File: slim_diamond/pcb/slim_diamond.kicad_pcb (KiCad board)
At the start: 2 copper layers, 87.4 x 92.1 mm, 25 parts, among them J1 JST PH 2.0 battery, SW1 pinky, SW10 index_bottom, SW11 thumb_outer, SW12 thumb_inner, SW13 MSK-12C02, SW2 ring_top, SW3 ring_home, SW4 ring_bottom, SW5 middle_top, SW6 middle_home, SW7 middle_bottom, SW8 index_top, SW9 index_home, U1 XIAO nRF52840

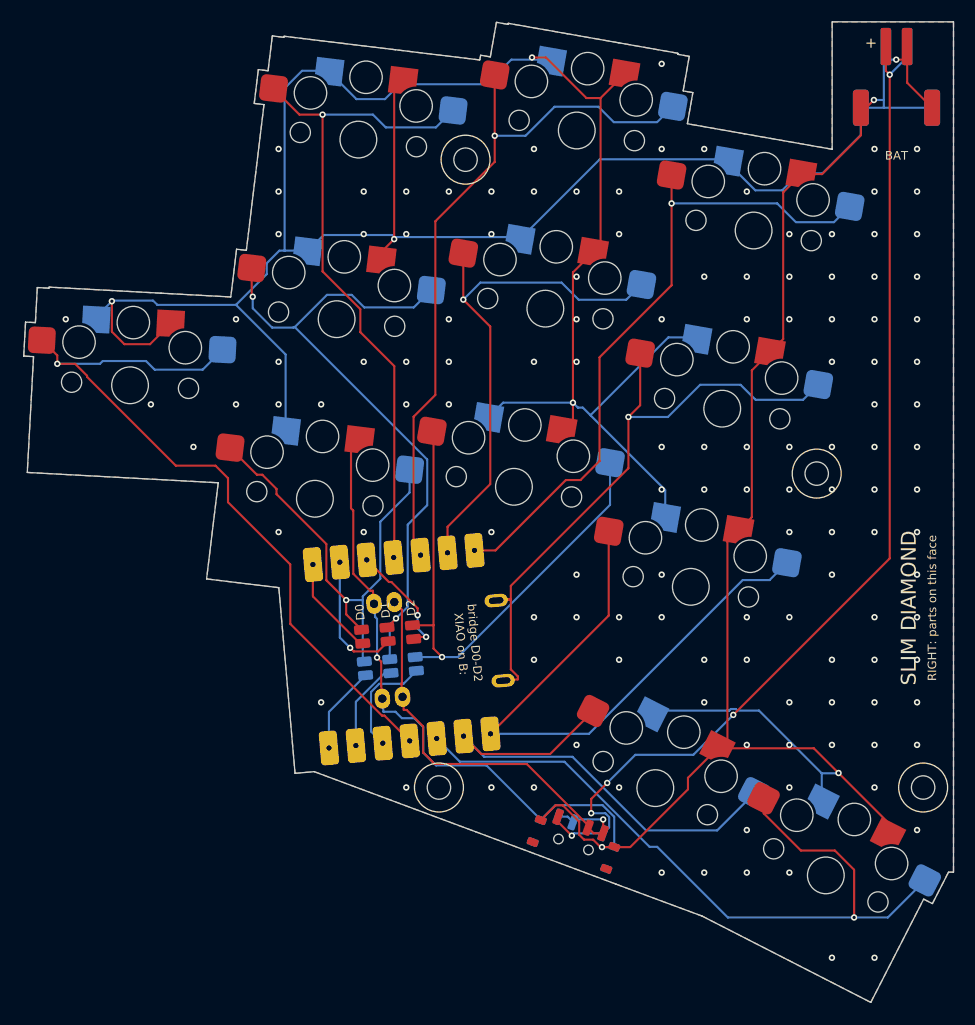
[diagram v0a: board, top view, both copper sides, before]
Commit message: Shape the Slim Diamond like a diamond, joined or stacked
Side by side, the joined halves are now a cut-diamond silhouette: the
fewest-facet convex outline around both halves, a table at the back and
pavilion facets down to the thumbs. The PCB follows it too. Stacked back
to back, the case walls lean in from a floor 2 mm wider than the rim, so
the pair reads as a cut gem from the side. Each half grows about 10%, the
PCB still fits JLC's 100 mm tier, and the tent stays at 6.6 degrees.

The Xiao and power switch move to the lower outer facet, with a routing
channel around both. A spot the router can't finish falls back to the
search's runners-up. The tent search now treats parts past the outermost
key as infeasible, and places the JST by least tent. New renders show
the halves joined and stacked.

Co-Authored-By: Claude Opus 5.5 <noreply@anthropic.com>
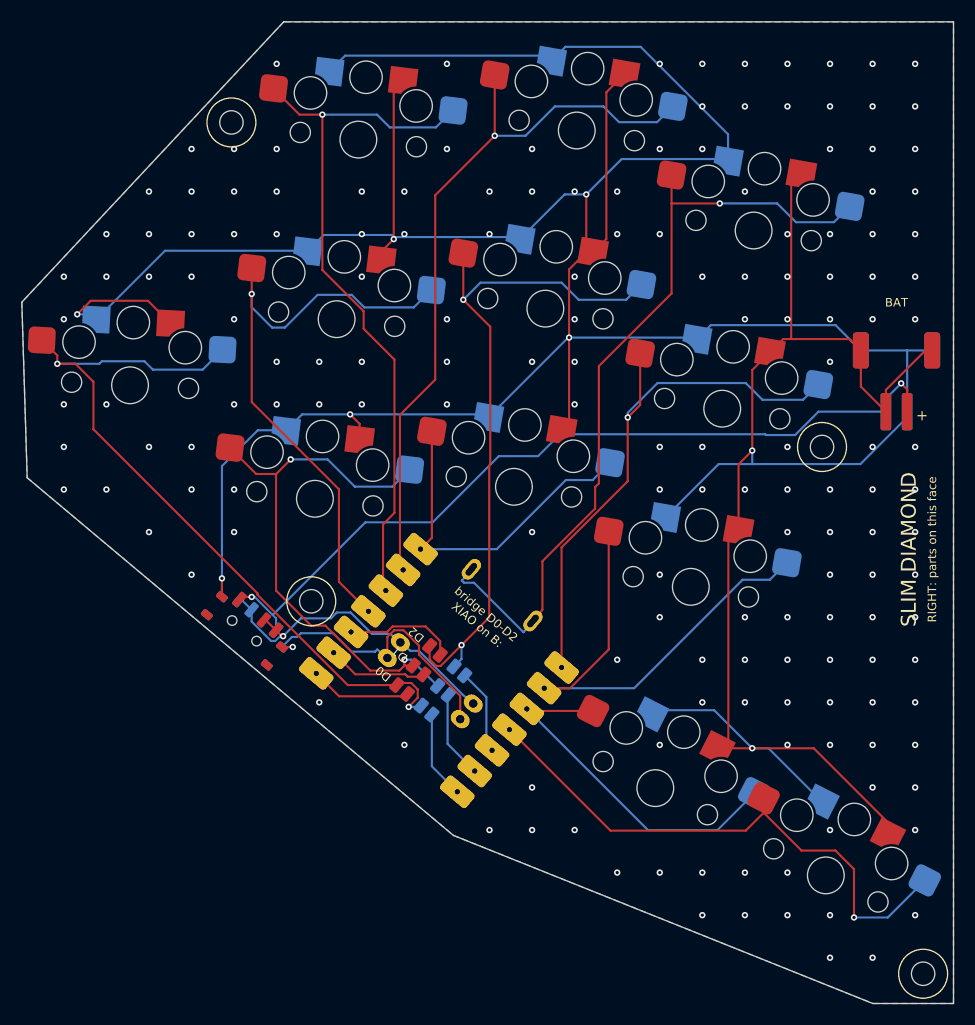
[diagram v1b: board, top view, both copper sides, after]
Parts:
- moved H4 49.0 mm to (78.0, 127.5)
- moved H3 48.2 mm to (126.0, 113.0)
- moved SW13 36.9 mm to (71.7, 130.3), turned to -40 degrees
- moved J1 28.6 mm to (133.0, 106.8), turned to 180 degrees
- moved H2 22.3 mm to (70.5, 82.5)
- moved H1 17.5 mm to (135.5, 162.5)
- moved JP14 6.99 mm to (88.8, 137.7), turned to 140 degrees
- moved JP1 6.23 mm to (86.5, 135.8), turned to 140 degrees
- moved JP13 5.44 mm to (90.4, 135.9), turned to 140 degrees
- moved JP2 4.43 mm to (88.1, 134.0), turned to 140 degrees
- moved JP12 4.15 mm to (91.9, 134.0), turned to 140 degrees
- moved U1 4.03 mm to (90.0, 134.0), turned to 140 degrees
- moved JP3 2.68 mm to (89.6, 132.1), turned to 140 degrees
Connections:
- JP1 pad 2: K_ring_bottom -> K_pinky
- JP12 pad 2: K_middle_bottom -> K_middle_home
- JP13 pad 2: K_ring_home -> K_ring_bottom
- JP14 pad 2: K_ring_bottom -> K_pinky
- JP2 pad 2: K_ring_home -> K_ring_bottom
- JP3 pad 2: K_middle_bottom -> K_middle_home
- U1 pad L10: K_thumb_inner -> K_thumb_outer
- U1 pad L11: K_pinky -> K_thumb_inner
- U1 pad L4: K_ring_top -> K_ring_home
- U1 pad L5: K_middle_top -> K_ring_top
- U1 pad L6: K_middle_home -> K_middle_top
- U1 pad L7: K_index_top -> K_middle_bottom
- U1 pad L8: K_index_bottom -> K_index_home
- U1 pad L9: K_thumb_outer -> K_index_bottom
- U1 pad NFC1: K_index_home -> K_index_top
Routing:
- net BAT+: track 99.3 -> 77.3 mm, vias 5 -> 2
- net K_middle_bottom: track 51.8 -> 32.7 mm, vias 1 -> 0
- net K_thumb_inner: track 70.9 -> 53.2 mm
- net K_middle_home: track 49.5 -> 65.3 mm, vias 1 -> 2
- net GND: track 467.8 -> 454.0 mm, vias 137 -> 174
- net K_thumb_outer: track 47.0 -> 33.8 mm
- net K_index_top: track 63.0 -> 75.9 mm
- net K_index_bottom: track 58.1 -> 46.4 mm
- net VBAT: track 41.4 -> 31.2 mm
- net K_ring_bottom: track 44.0 -> 52.0 mm, vias 1 -> 2
- net K_index_home: track 60.4 -> 53.3 mm
- net K_ring_home: track 62.8 -> 58.1 mm, vias 2 -> 1
- net K_ring_top: track 63.5 -> 67.1 mm
- net X_L2: track 12.6 -> 9.49 mm, vias 1 -> 0
- net X_L12: track 10.4 -> 8.11 mm
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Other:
- board size 87.4 x 92.1 mm -> 87.6 x 92.3 mm

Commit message: Use M3 self-tapping screws for the Slim Diamond case
The case will be printed in Nylon, which takes a self-tapped thread well,
so the screws move up to M3 button heads (ISO 7380) in 6 mm standoffs
with 2.5 mm pilot holes. M3 x 6 is the longest that fits the short
standoffs on the outer side. The screw lives in one SCREW setting in
design.py; the hole search, the footprint and the case read it from
there, so switching to heat-set inserts is a one-line change.

Co-Authored-By: Claude Opus 5.5 <noreply@anthropic.com>
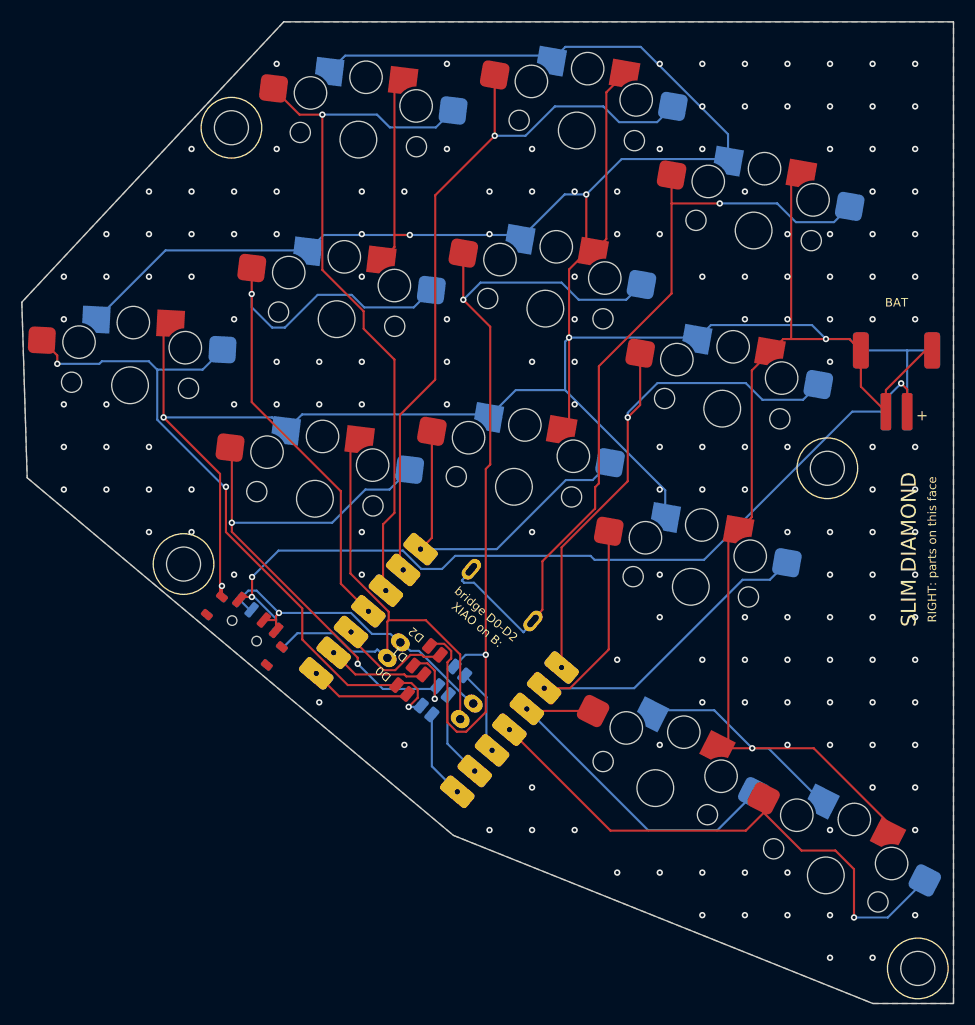
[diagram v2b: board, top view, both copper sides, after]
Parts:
- H1, H2, H3, H4: value M2 -> M3; footprint slim_diamond:MountingHole_M2 -> slim_diamond:MountingHole_M3
- moved H4 12.5 mm to (66.0, 124.0)
- moved H3 2.06 mm to (126.5, 115.0)
- moved H1 0.71 mm to (135.0, 162.0)
- moved H2 0.50 mm to (70.5, 83.0)
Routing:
- net GND: track 454.0 -> 471.4 mm, vias 174 -> 171
- net K_middle_home: track 65.3 -> 80.4 mm
- net K_ring_bottom: track 52.0 -> 58.6 mm, vias 2 -> 3
- net K_pinky: track 72.2 -> 66.8 mm, vias 2 -> 3
- net BAT+: track 77.3 -> 81.3 mm, vias 2 -> 3
